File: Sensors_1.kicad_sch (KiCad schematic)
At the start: 24 parts, among them U10 LSM6DS3, U11 MPU-6500, U12 BMI270, U3 Ai-Thinker-Ra-01, U8 AT24C256, U9 Ai-Thinker-Ra-01SH

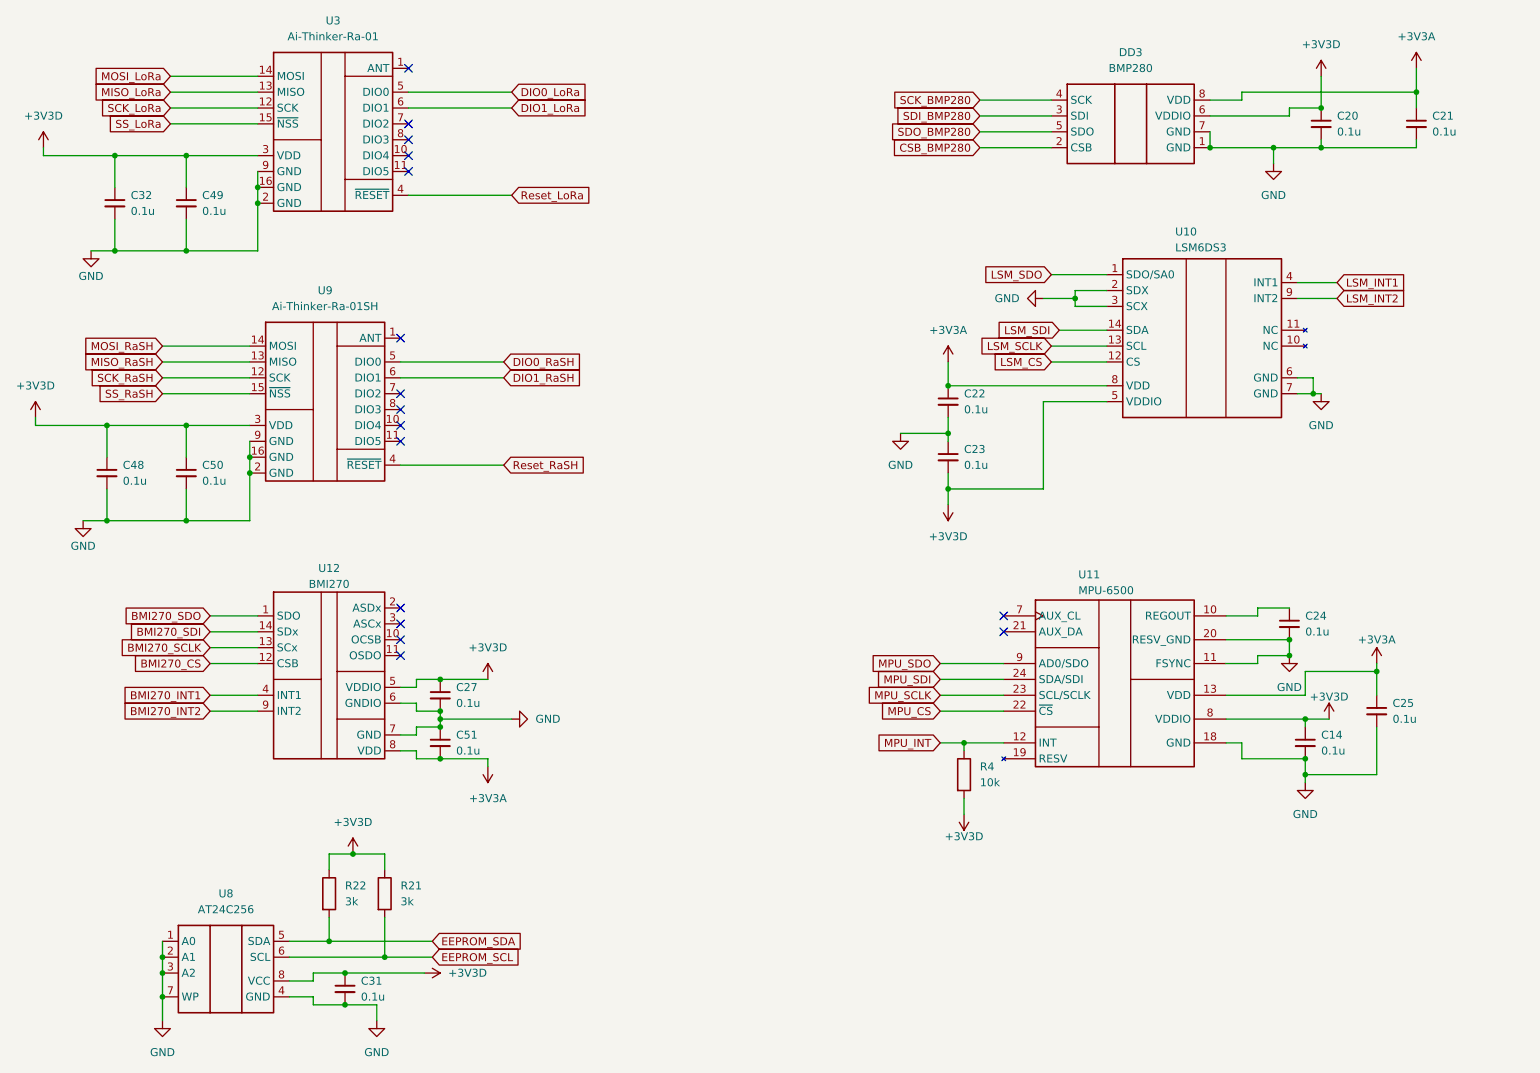
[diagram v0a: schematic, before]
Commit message: feat:убрал часть с батарейным питанием, убрал лишние элементы со старого проекта
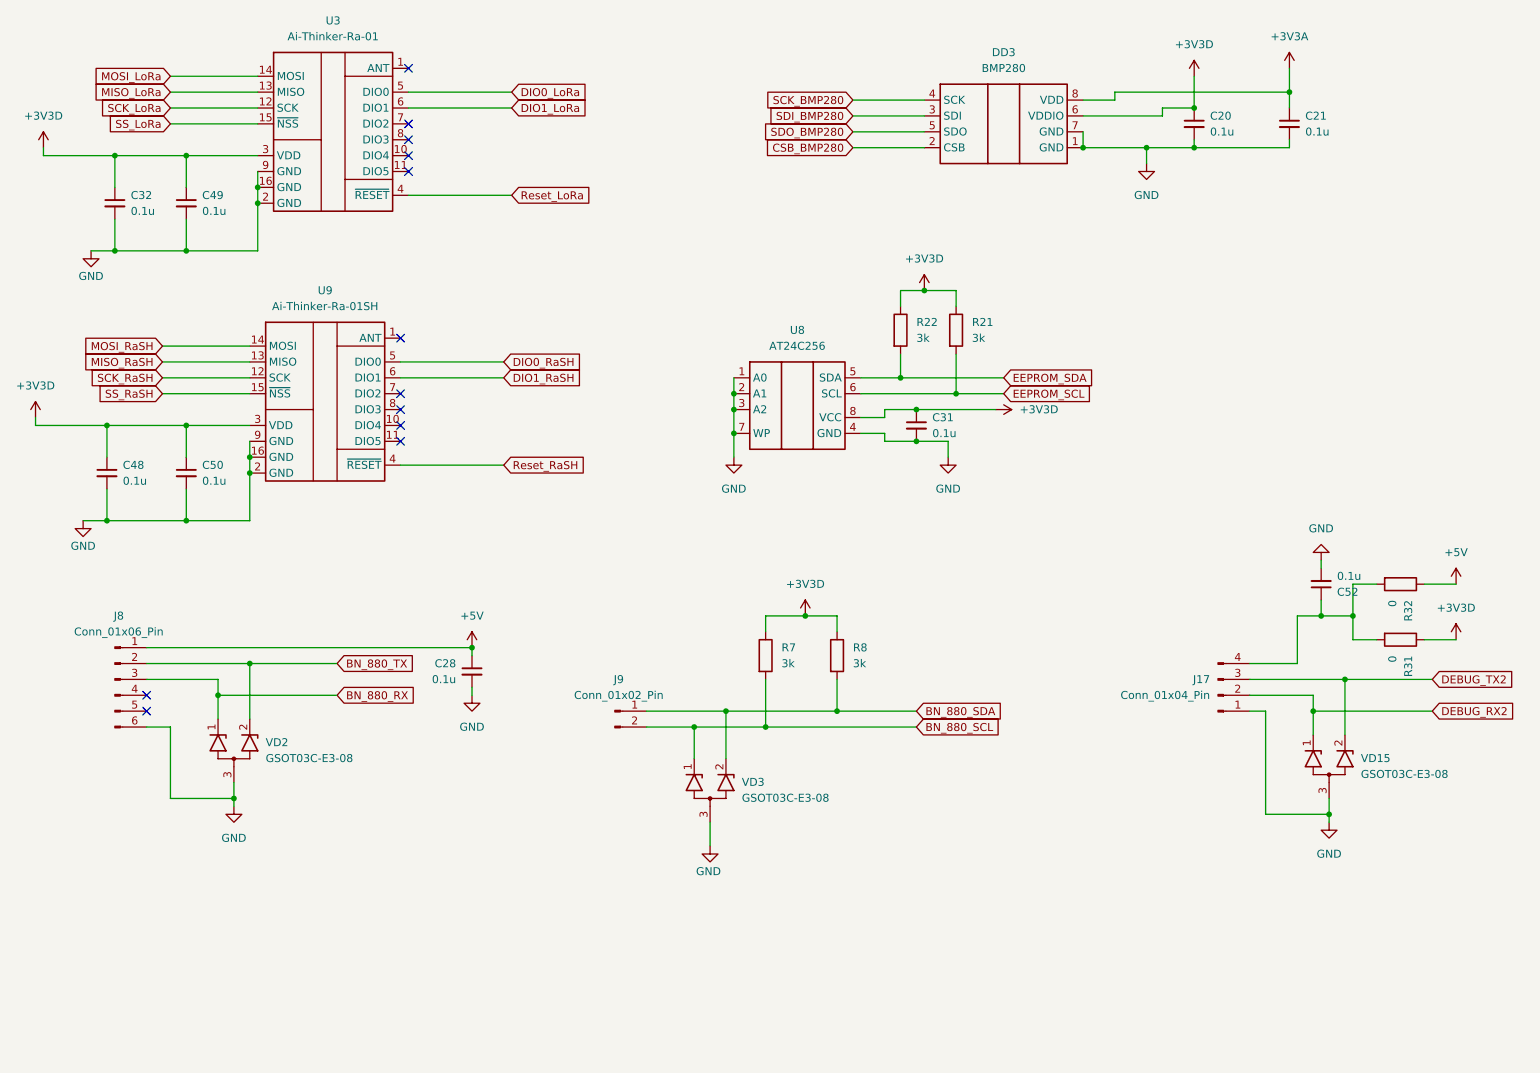
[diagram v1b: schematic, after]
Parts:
- removed C14, C22, C23, C24, C25, C27, C51: 0.1u, Capacitor_SMD:C_0805_2012Metric_Pad1.18x1.45mm_HandSolder, symbol Device:C_Small
- removed R4: 10k, Resistor_SMD:R_0805_2012Metric_Pad1.20x1.40mm_HandSolder, symbol Device:R
- removed U10: LSM6DS3, Package_LGA:LGA-14_3x2.5mm_P0.5mm_LayoutBorder3x4y, symbol Sensor_Motion:LSM6DS3
- removed U11: MPU-6500, Sensor_Motion:InvenSense_QFN-24_3x3mm_P0.4mm, symbol Sensor_Motion:MPU-9250
- removed U12: BMI270, Package_LGA:Bosch_LGA-14_3x2.5mm_P0.5mm, symbol IMU:BMI270
- added C28, C52: 0.1u, Capacitor_SMD:C_0805_2012Metric_Pad1.18x1.45mm_HandSolder, symbol Device:C_Small
- added J17: Conn_01x04_Pin, Connector_PinSocket_2.54mm:PinSocket_1x04_P2.54mm_Vertical, symbol Connector:Conn_01x04_Pin
- added J8: Conn_01x06_Pin, Connector_Hirose:Hirose_DF13-06P-1.25DSA_1x06_P1.25mm_Vertical, symbol Connector:Conn_01x06_Pin
- added J9: Conn_01x02_Pin, Connector_Hirose:Hirose_DF13-02P-1.25DSA_1x02_P1.25mm_Vertical, symbol Connector:Conn_01x02_Pin
- added R31, R32: 0, Resistor_SMD:R_0805_2012Metric_Pad1.20x1.40mm_HandSolder, symbol Device:R
- added R7, R8: 3k, Resistor_SMD:R_0805_2012Metric_Pad1.20x1.40mm_HandSolder, symbol Device:R
- added VD15, VD2, VD3: GSOT03C-E3-08, Package_TO_SOT_SMD:SOT-23, symbol TWS:GSOT03C-E3-08
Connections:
- net +3V3D: now also R31.1, R7.1, R8.1
- net GND: now also C28.2, C52.2, J17.1 (Pin_1), J8.6 (Pin_6), VD15.3 (A), VD2.3 (A), VD3.3 (A)
- new net: C52.1, J17.4 (Pin_4), R31.2, R32.2
- new net +5V: C28.1, J8.1 (Pin_1), R32.1
- new net BN_880_RX: J8.3 (Pin_3), VD2.1 (K1)
- new net BN_880_SCL: J9.2 (Pin_2), R7.2, VD3.1 (K1)
- new net BN_880_SDA: J9.1 (Pin_1), R8.2, VD3.2 (K2)
- new net BN_880_TX: J8.2 (Pin_2), VD2.2 (K2)
- new net DEBUG_RX2: J17.2 (Pin_2), VD15.1 (K1)
- new net DEBUG_TX2: J17.3 (Pin_3), VD15.2 (K2)
- no-connect marks 16 -> 12
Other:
- moved on the sheet: C20, C21, C31, DD3, R21, R22, U8

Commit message: feaat: добавлены светодиоды, кнопки и недостающие элементы защиты питания
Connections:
- net +3V3D: no longer R31.1
- new net +3V3: R31.1
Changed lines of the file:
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@@
 			)
 		)
-		(property "Value" "+3V3D"
+		(property "Value" "+3V3"
 			(at 255.27 116.84 0)
 			(show_name no)

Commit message: feat: добавлены глобальные линии связи, удалены линии связи со старого проекта
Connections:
- net DEBUG_RX2 renamed DEBUG_RX1
- net DEBUG_TX2 renamed DEBUG_TX1
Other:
- moved on the sheet: C52
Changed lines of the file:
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@@
 	)
 	(junction
-		(at 233.68 118.11)
+		(at 229.87 118.11)
 		(diameter 0)
 		(color 0 0 0 0)
@@
 	(wire
 		(pts
-			(xy 233.68 110.49) (xy 233.68 109.22)
+			(xy 229.87 110.49) (xy 229.87 109.22)
 		)
 		(stroke
@@
 	(wire
 		(pts
-			(xy 233.68 118.11) (xy 238.76 118.11)
+			(xy 229.87 118.11) (xy 238.76 118.11)
 		)
 		(stroke
@@
 	(wire
 		(pts
-			(xy 229.87 118.11) (xy 233.68 118.11)
-		)
-		(stroke
-			(width 0)
-			(type default)
-		)
-	)
-	(wire
-		(pts
 			(xy 208.28 38.1) (xy 208.28 36.83)
 		)
@@
 	(wire
 		(pts
-			(xy 233.68 115.57) (xy 233.68 118.11)
+			(xy 229.87 115.57) (xy 229.87 118.11)
 		)
 		(stroke
@@
 		)
 	)
-	(global_label "DEBUG_RX2"
+	(global_label "DEBUG_RX1"
 		(shape input)
 		(at 251.46 133.35 0)
@@
 		)
 	)
-	(global_label "DEBUG_TX2"
+	(global_label "DEBUG_TX1"
 		(shape input)
 		(at 251.46 128.27 0)
@@
 	(symbol
 		(lib_id "Device:C_Small")
-		(at 233.68 113.03 0)
+		(at 229.87 113.03 0)
 		(mirror x)
 		(unit 1)
@@
 		(fields_autoplaced yes)
 		(property "Reference" "C52"
-			(at 236.22 114.2938 0)
+			(at 232.41 114.2938 0)
 			(show_name no)
 			(do_not_autoplace no)
@@
 		)
 		(property "Value" "0.1u"
-			(at 236.22 111.7538 0)
+			(at 232.41 111.7538 0)
 			(show_name no)
 			(do_not_autoplace no)
@@
 		)
 		(property "Footprint" "Capacitor_SMD:C_0805_2012Metric_Pad1.18x1.45mm_HandSolder"
-			(at 233.68 113.03 0)
+			(at 229.87 113.03 0)
 			(hide yes)
 			(show_name no)
@@
 		)
 		(property "Datasheet" ""
-			(at 233.68 113.03 0)
+			(at 229.87 113.03 0)
 			(hide yes)
 			(show_name no)
@@
 		)
 		(property "Description" "Unpolarized capacitor, small symbol"
-			(at 233.68 113.03 0)
+			(at 229.87 113.03 0)
 			(hide yes)
 			(show_name no)
@@
 	(symbol
 		(lib_id "power:GND")
-		(at 233.68 109.22 0)
+		(at 229.87 109.22 0)
 		(mirror x)
 		(unit 1)
@@
 		(fields_autoplaced yes)
 		(property "Reference" "#PWR0110"
-			(at 233.68 102.87 0)
+			(at 229.87 102.87 0)
 			(hide yes)
 			(show_name no)
@@
 		)
 		(property "Value" "GND"
-			(at 233.68 104.14 0)
+			(at 229.87 104.14 0)
 			(show_name no)
 			(do_not_autoplace no)
@@
 		)
 		(property "Footprint" ""
-			(at 233.68 109.22 0)
+			(at 229.87 109.22 0)
 			(hide yes)
 			(show_name no)
@@
 		)
 		(property "Datasheet" ""
-			(at 233.68 109.22 0)
+			(at 229.87 109.22 0)
 			(hide yes)
 			(show_name no)
@@
 		)
 		(property "Description" "Power symbol creates a global label with name \"GND\" , ground"
-			(at 233.68 109.22 0)
+			(at 229.87 109.22 0)
 			(hide yes)
 			(show_name no)

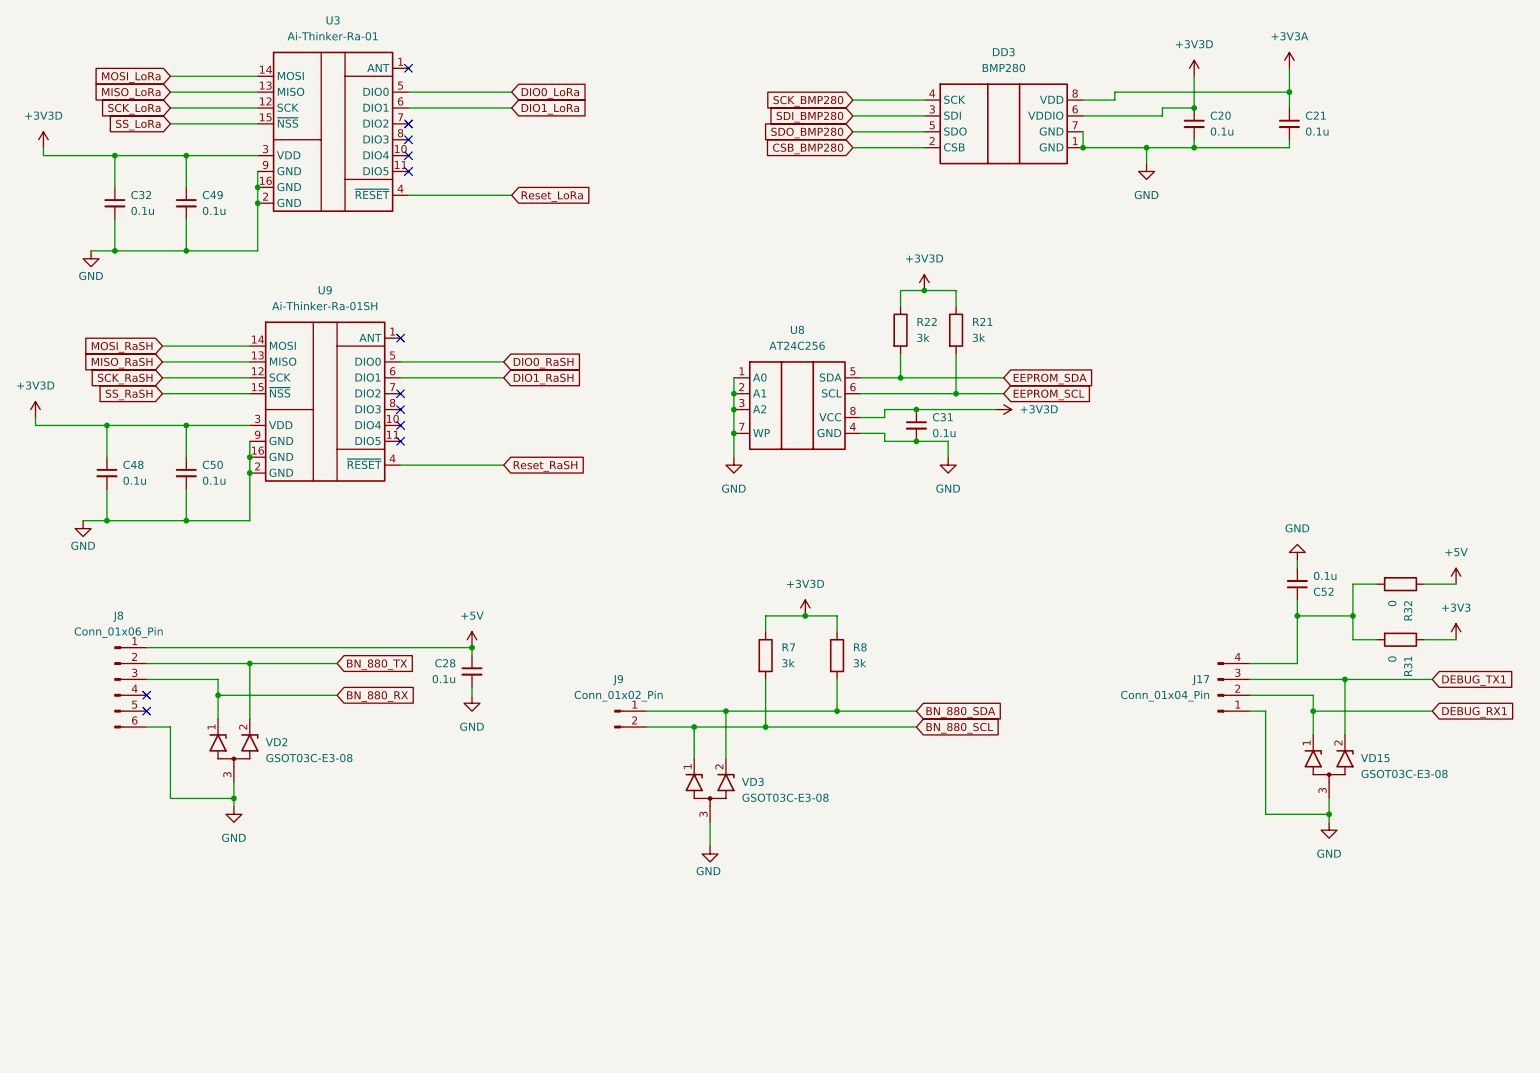
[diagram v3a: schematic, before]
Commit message: feat: расположены основные узлы модуля на печатной плате
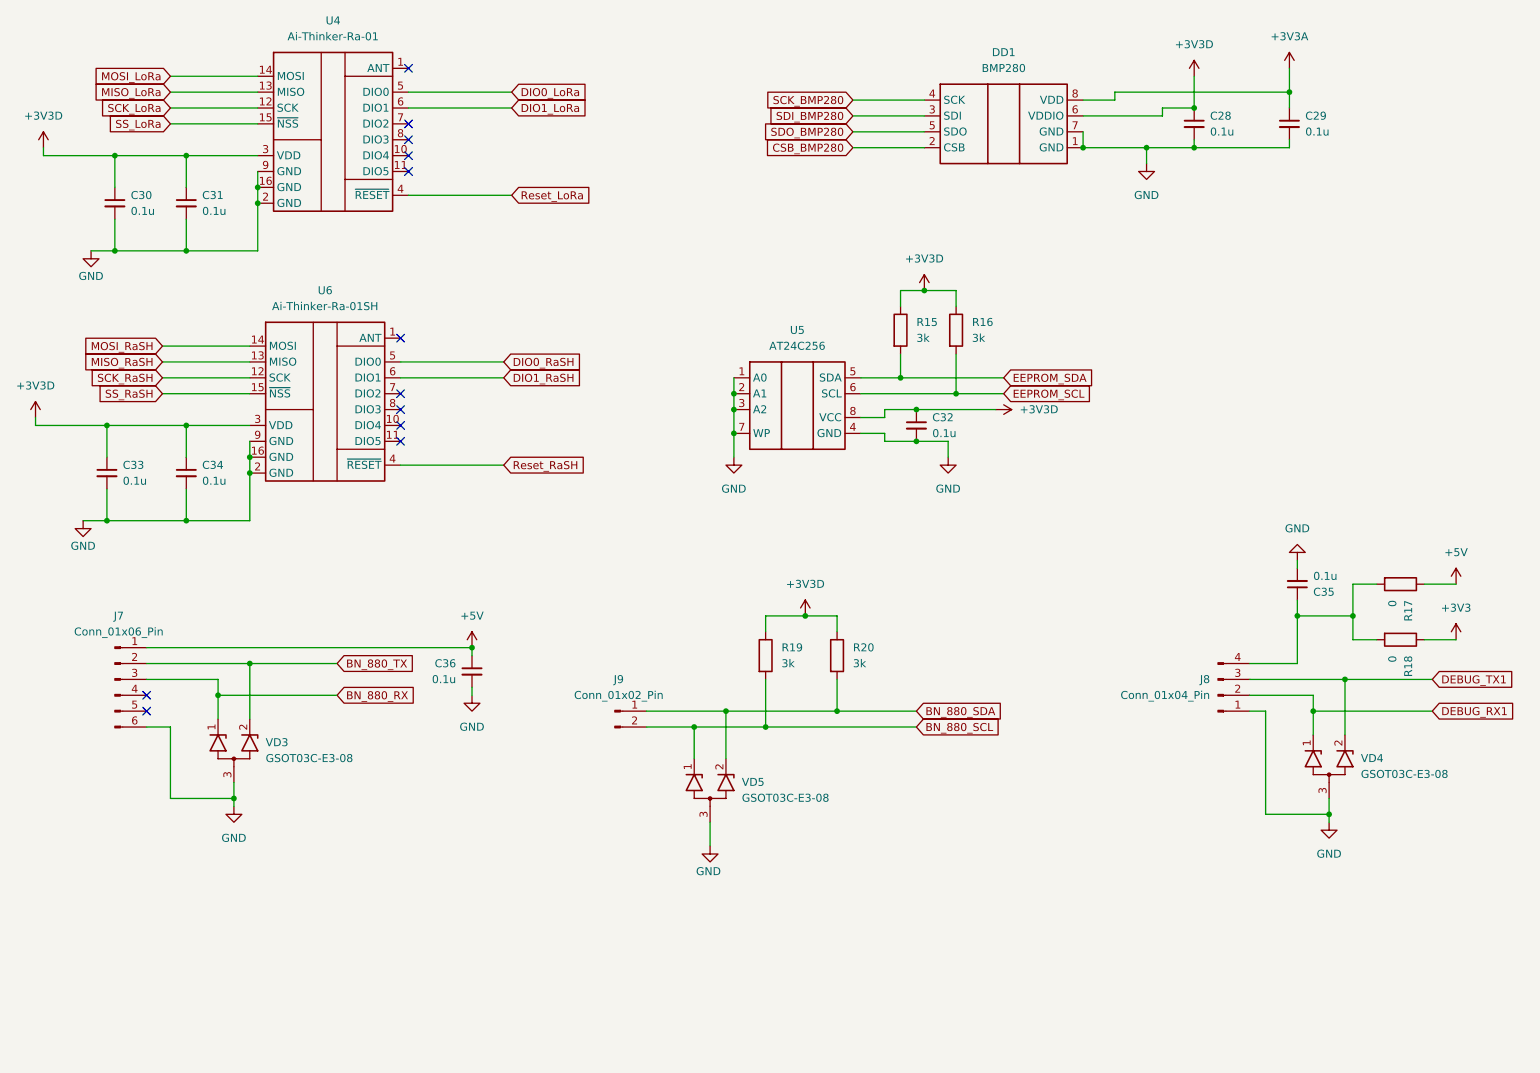
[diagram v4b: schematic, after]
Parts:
- renumbered C20 to C28, C21 to C29, C32 to C30, C49 to C31, C31 to C32, C48 to C33, C50 to C34, C52 to C35, C28 to C36, DD3 to DD1, J8 to J7, J17 to J8, R22 to R15, R21 to R16, R32 to R17, R31 to R18, R7 to R19, R8 to R20, U3 to U4, U8 to U5, U9 to U6, VD2 to VD3, VD15 to VD4, VD3 to VD5

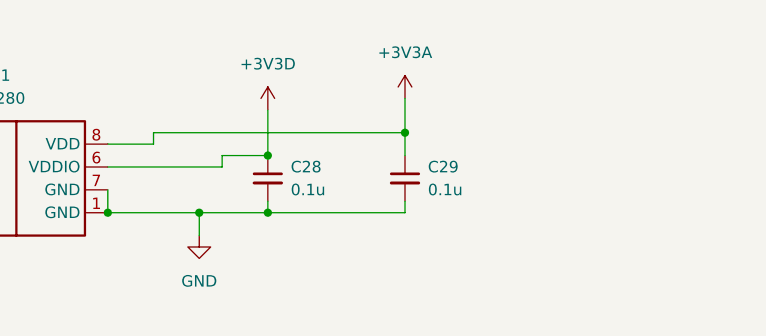
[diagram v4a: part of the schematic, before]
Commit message: feat: добавлена обвязка внешних интерфейсов
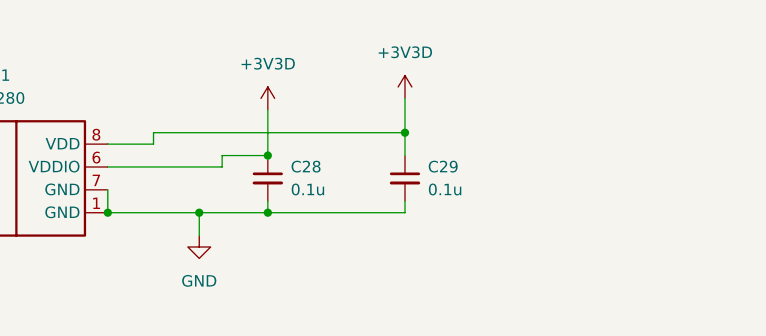
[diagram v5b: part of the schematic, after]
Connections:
- net +3V3A is gone; now on net +3V3D: C29.1, DD1.8 (VDD)
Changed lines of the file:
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@@
-	)
-	(symbol
-		(lib_id "power:+5V")
-		(at 228.6 30.48 0)
-		(unit 1)
-		(body_style 1)
-		(exclude_from_sim no)
-		(in_bom yes)
-		(on_board yes)
-		(in_pos_files yes)
-		(dnp no)
-		(fields_autoplaced yes)
-		(property "Reference" "#PWR050"
-			(at 228.6 34.29 0)
-			(hide yes)
-			(show_name no)
-			(do_not_autoplace no)
-			(effects
-				(font
-					(size 1.27 1.27)
-				)
-			)
-		)
-		(property "Value" "+3V3A"
-			(at 228.6 25.4 0)
-			(show_name no)
-			(do_not_autoplace no)
-			(effects
-				(font
-					(size 1.27 1.27)
-				)
-			)
-		)
-		(property "Footprint" ""
-			(at 228.6 30.48 0)
-			(hide yes)
-			(show_name no)
-			(do_not_autoplace no)
-			(effects
-				(font
-					(size 1.27 1.27)
-				)
-			)
-		)
-		(property "Datasheet" ""
-			(at 228.6 30.48 0)
-			(hide yes)
-			(show_name no)
-			(do_not_autoplace no)
-			(effects
-				(font
-					(size 1.27 1.27)
-				)
-			)
-		)
-		(property "Description" "Power symbol creates a global label with name \"+5V\""
-			(at 228.6 30.48 0)
-			(hide yes)
-			(show_name no)
-			(do_not_autoplace no)
-			(effects
-				(font
-					(size 1.27 1.27)
-				)
-			)
-		)
-		(pin "1"
-		)
-		(instances
-			(project "Magister_work_v1"
-				(path "/9ff4e5e8-ab59-4c4d-a10a-f8f5e444c5cb/08b35b78-346e-4aaf-94c2-29c106b914b4"
-					(reference "#PWR050")
-					(unit 1)
-				)
-			)
-		)
 	)
 	(symbol
@@
 					(unit 1)
 				)
+			)
+		)
+	)
+	(symbol
+		(lib_id "power:+5V")
+		(at 228.6 30.48 0)
+		(unit 1)
+		(body_style 1)
+		(exclude_from_sim no)
+		(in_bom yes)
+		(on_board yes)
+		(in_pos_files yes)
+		(dnp no)
+		(fields_autoplaced yes)
+		(property "Reference" "#PWR078"
+			(at 228.6 34.29 0)
+			(hide yes)
+			(show_name no)
+			(do_not_autoplace no)
+			(effects
+				(font
+					(size 1.27 1.27)
+				)
+			)
+		)
+		(property "Value" "+3V3D"
+			(at 228.6 25.4 0)
+			(show_name no)
+			(do_not_autoplace no)
+			(effects
+				(font
+					(size 1.27 1.27)
+				)
+			)
+		)
+		(property "Footprint" ""
+			(at 228.6 30.48 0)
+			(hide yes)
+			(show_name no)
+			(do_not_autoplace no)
+			(effects
+				(font
+					(size 1.27 1.27)
+				)
+			)
+		)
+		(property "Datasheet" ""
+			(at 228.6 30.48 0)
+			(hide yes)
+			(show_name no)
+			(do_not_autoplace no)
+			(effects
+				(font
+					(size 1.27 1.27)
+				)
+			)
+		)
+		(property "Description" "Power symbol creates a global label with name \"+5V\""
+			(at 228.6 30.48 0)
+			(hide yes)
+			(show_name no)
+			(do_not_autoplace no)
+			(effects
+				(font
+					(size 1.27 1.27)
+				)
+			)
+		)
+		(pin "1"
+		)
+		(instances
+			(project "Magister_work_v1"
+				(path "/9ff4e5e8-ab59-4c4d-a10a-f8f5e444c5cb/08b35b78-346e-4aaf-94c2-29c106b914b4"
+					(reference "#PWR078")
+					(unit 1)
+				)
